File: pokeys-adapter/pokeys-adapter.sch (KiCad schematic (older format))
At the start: 6 parts, among them J1 Bus, J2 PinHeader_01x12, J3 PinHeader_01x12, J4 Screw_Terminal_01x02, J5 Mounting hole, J6 Mounting hole

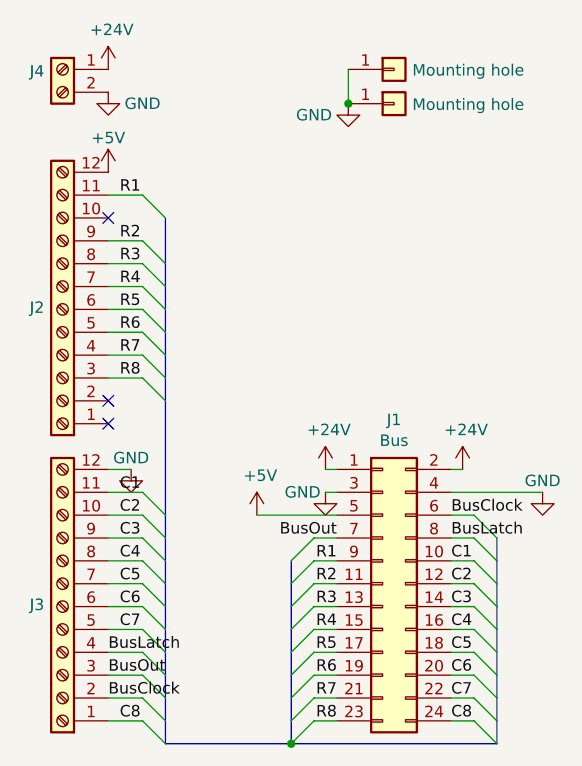
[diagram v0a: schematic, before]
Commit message: Add power flags
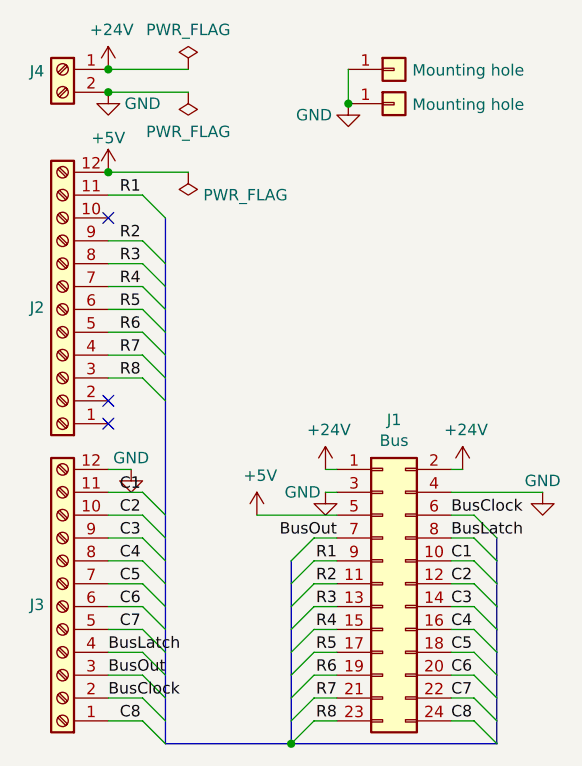
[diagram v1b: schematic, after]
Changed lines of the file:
@@
 	-1   0    0    1
 $EndComp
-Wire Bus Line
-	2750 1650 2750 3950
-Wire Bus Line
-	4200 3050 4200 3950
-Wire Bus Line
-	3300 3150 3300 3950
 $Comp
 L Connector:Screw_Terminal_01x12 J2
@@
 	-1   0    0    1
 $EndComp
+$Comp
+L power:PWR_FLAG #FLG0101
+U 1 1 5F74C8C7
+P 2850 1000
+F 0 "#FLG0101" H 2850 1075 50  0001 C CNN
+F 1 "PWR_FLAG" H 2850 1173 50  0000 C CNN
+F 2 "" H 2850 1000 50  0001 C CNN
+F 3 "~" H 2850 1000 50  0001 C CNN
+	1    2850 1000
+	1    0    0    -1
+$EndComp
+$Comp
+L power:PWR_FLAG #FLG0102
+U 1 1 5F74CDAF
+P 2850 1100
+F 0 "#FLG0102" H 2850 1175 50  0001 C CNN
+F 1 "PWR_FLAG" H 2850 1273 50  0000 C CNN
+F 2 "" H 2850 1100 50  0001 C CNN
+F 3 "~" H 2850 1100 50  0001 C CNN
+	1    2850 1100
+	-1   0    0    1
+$EndComp
+Wire Wire Line
+	2500 1100 2850 1100
+Connection ~ 2500 1100
+Wire Wire Line
+	2500 1000 2850 1000
+Connection ~ 2500 1000
+$Comp
+L power:PWR_FLAG #FLG0103
+U 1 1 5F7534F4
+P 2850 1450
+F 0 "#FLG0103" H 2850 1525 50  0001 C CNN
+F 1 "PWR_FLAG" H 2600 1550 50  0000 C CNN
+F 2 "" H 2850 1450 50  0001 C CNN
+F 3 "~" H 2850 1450 50  0001 C CNN
+	1    2850 1450
+	-1   0    0    1
+$EndComp
+Wire Wire Line
+	2500 1450 2850 1450
+Wire Bus Line
+	4200 3050 4200 3950
+Wire Bus Line
+	3300 3150 3300 3950
+Wire Bus Line
+	2750 1650 2750 3950
+Connection ~ 2500 1450
 $EndSCHEMATC
